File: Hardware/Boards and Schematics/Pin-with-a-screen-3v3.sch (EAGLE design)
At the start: 29 parts, among them J1 AVR_SPI_PRG_6NS, Q1 MMBT2222A, Q2 BL8530, U1 ATMEGA328P, U2 MICRO-SD-SOCKET-SMD1:1, Y1 8MHz

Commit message: Removed transistor-resistor logic level shifter
Logic level shifter was used for PWM-ing backlight signal for screen.
Since MCU operates on 3v3 logic like screen, level shifter is not
necessary.
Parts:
- removed Q1: MMBT2222A, SparkFun-DiscreteSemi:TRANSISTOR_NPNMMBT2222A
- removed R3: 1k, SparkFun-Passives:RESISTOR0603-RES
- removed R4: 22R, SparkFun-Passives:RESISTOR0603-RES
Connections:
- removed net LEDK: LCD2.LEDK, R4.2
- removed net TRAN_BASE: Q1.B, R3.2
- removed net TRAN_COLLECTOR: Q1.C, R4.1
- net GND: no longer Q1.E
- net TFT_BACKLIGHT: now also LCD2.LEDK; no longer R3.1
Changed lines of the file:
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@@
 <part name="C3" library="SparkFun" deviceset="CAP" device="0603-CAP" value="0.1uF"/>
 <part name="C4" library="SparkFun" deviceset="CAP" device="0603-CAP" value="0.1uF"/>
-<part name="Q1" library="SparkFun-DiscreteSemi" deviceset="TRANSISTOR_NPN" device="MMBT2222A" value="MMBT2222A"/>
-<part name="R3" library="SparkFun-Passives" deviceset="RESISTOR" device="0603-RES" value="1k"/>
-<part name="R4" library="SparkFun-Passives" deviceset="RESISTOR" device="0603-RES" value="22R"/>
-<part name="GND2" library="SparkFun-Aesthetics" deviceset="GND" device=""/>
 <part name="GND3" library="SparkFun-Aesthetics" deviceset="GND" device=""/>
 <part name="SUPPLY2" library="SparkFun-Aesthetics" deviceset="3.3V" device=""/>
@@
 <instance part="C3" gate="G$1" x="-119.38" y="154.94"/>
 <instance part="C4" gate="G$1" x="-104.14" y="154.94"/>
-<instance part="Q1" gate="G$1" x="-43.18" y="60.96" rot="MR0"/>
-<instance part="R3" gate="G$1" x="-35.56" y="68.58" rot="R180"/>
-<instance part="R4" gate="G$1" x="-71.12" y="66.04" rot="R180"/>
-<instance part="GND2" gate="1" x="-45.72" y="50.8"/>
 <instance part="GND3" gate="1" x="-111.76" y="147.32"/>
 <instance part="SUPPLY2" gate="G$1" x="-111.76" y="162.56"/>
@@
 <net name="GND" class="0">
 <segment>
-<pinref part="Q1" gate="G$1" pin="E"/>
-<pinref part="GND2" gate="1" pin="GND"/>
-<wire x1="-45.72" y1="55.88" x2="-45.72" y2="53.34" width="0.1524" layer="91"/>
-</segment>
-<segment>
 <pinref part="C3" gate="G$1" pin="2"/>
 <wire x1="-119.38" y1="152.4" x2="-119.38" y2="149.86" width="0.1524" layer="91"/>
@@
 </segment>
 </net>
-<net name="TRAN_COLLECTOR" class="0">
-<segment>
-<pinref part="R4" gate="G$1" pin="1"/>
-<pinref part="Q1" gate="G$1" pin="C"/>
-<wire x1="-66.04" y1="66.04" x2="-45.72" y2="66.04" width="0.1524" layer="91"/>
-</segment>
-</net>
-<net name="TRAN_BASE" class="0">
-<segment>
-<pinref part="R3" gate="G$1" pin="2"/>
-<pinref part="Q1" gate="G$1" pin="B"/>
-<wire x1="-40.64" y1="68.58" x2="-40.64" y2="60.96" width="0.1524" layer="91"/>
-</segment>
-</net>
 <net name="N$3" class="0">
 <segment>
@@
 </segment>
 <segment>
-<pinref part="R3" gate="G$1" pin="1"/>
-<wire x1="-30.48" y1="68.58" x2="-17.78" y2="68.58" width="0.1524" layer="91"/>
-<label x="-20.32" y="68.58" size="1.778" layer="95"/>
-</segment>
-</net>
-<net name="LEDK" class="0">
-<segment>
 <pinref part="LCD2" gate="G$1" pin="LEDK"/>
 <wire x1="-86.36" y1="48.26" x2="-76.2" y2="48.26" width="0.1524" layer="91"/>
-<wire x1="-76.2" y1="48.26" x2="-76.2" y2="66.04" width="0.1524" layer="91"/>
-<pinref part="R4" gate="G$1" pin="2"/>
-</segment>
-</net>
+<wire x1="-76.2" y1="48.26" x2="-76.2" y2="60.96" width="0.1524" layer="91"/>
+<wire x1="-76.2" y1="60.96" x2="-66.04" y2="60.96" width="0.1524" layer="91"/>
+<label x="-66.04" y="60.96" size="1.778" layer="95"/>
+</segment>
+</net>

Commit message: Changed led to red and series resistor to 51R
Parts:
- BLINKY: value Green -> Red
- R1: value 5R -> 51R
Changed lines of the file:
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@@
 <part name="SUPPLY9" library="SparkFun-Aesthetics" deviceset="3.3V" device=""/>
 <part name="GND9" library="SparkFun-Aesthetics" deviceset="GND" device=""/>
-<part name="R1" library="SparkFun-Passives" deviceset="RESISTOR" device="0603-RES" value="5R"/>
-<part name="BLINKY" library="SparkFun" deviceset="LED" device="0603" value="Green"/>
+<part name="R1" library="SparkFun-Passives" deviceset="RESISTOR" device="0603-RES" value="51R"/>
+<part name="BLINKY" library="SparkFun" deviceset="LED" device="0603" value="Red"/>
 <part name="GND13" library="SparkFun-Aesthetics" deviceset="GND" device=""/>
 <part name="PAD1" library="wirepad" deviceset="2,15/1,0" device=""/>

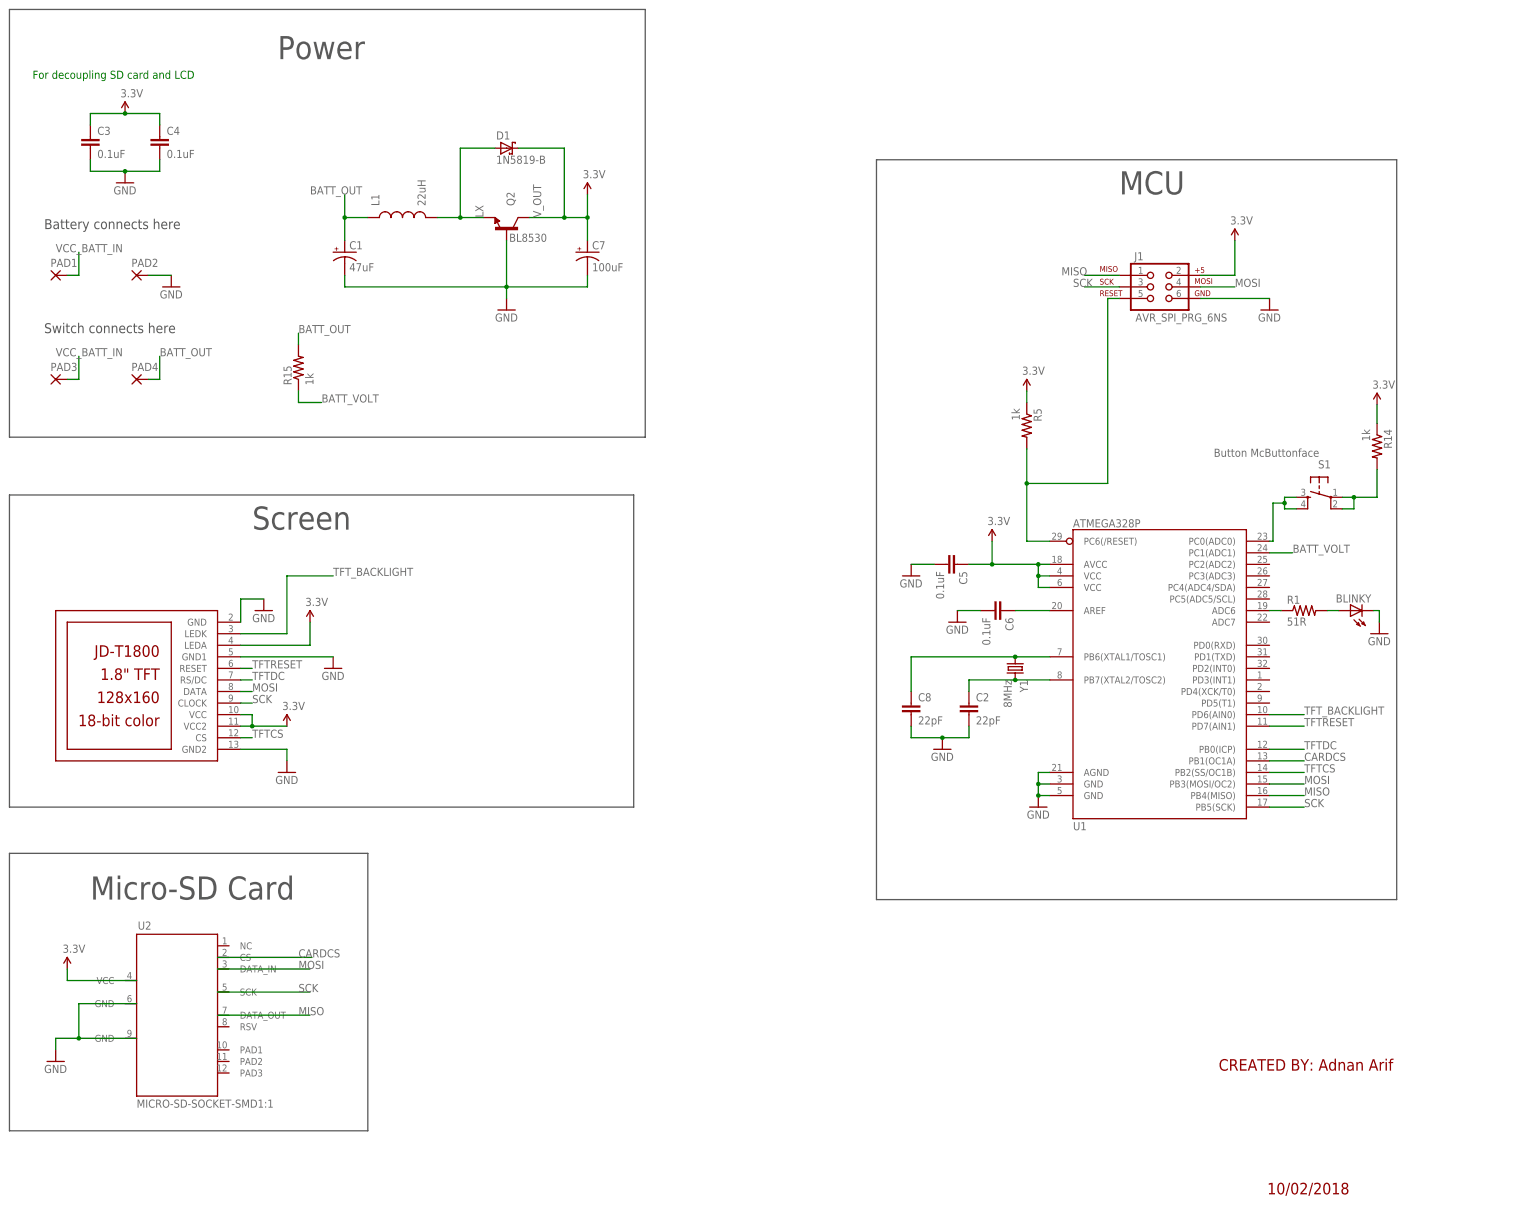
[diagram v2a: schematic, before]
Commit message: Added protoboard section
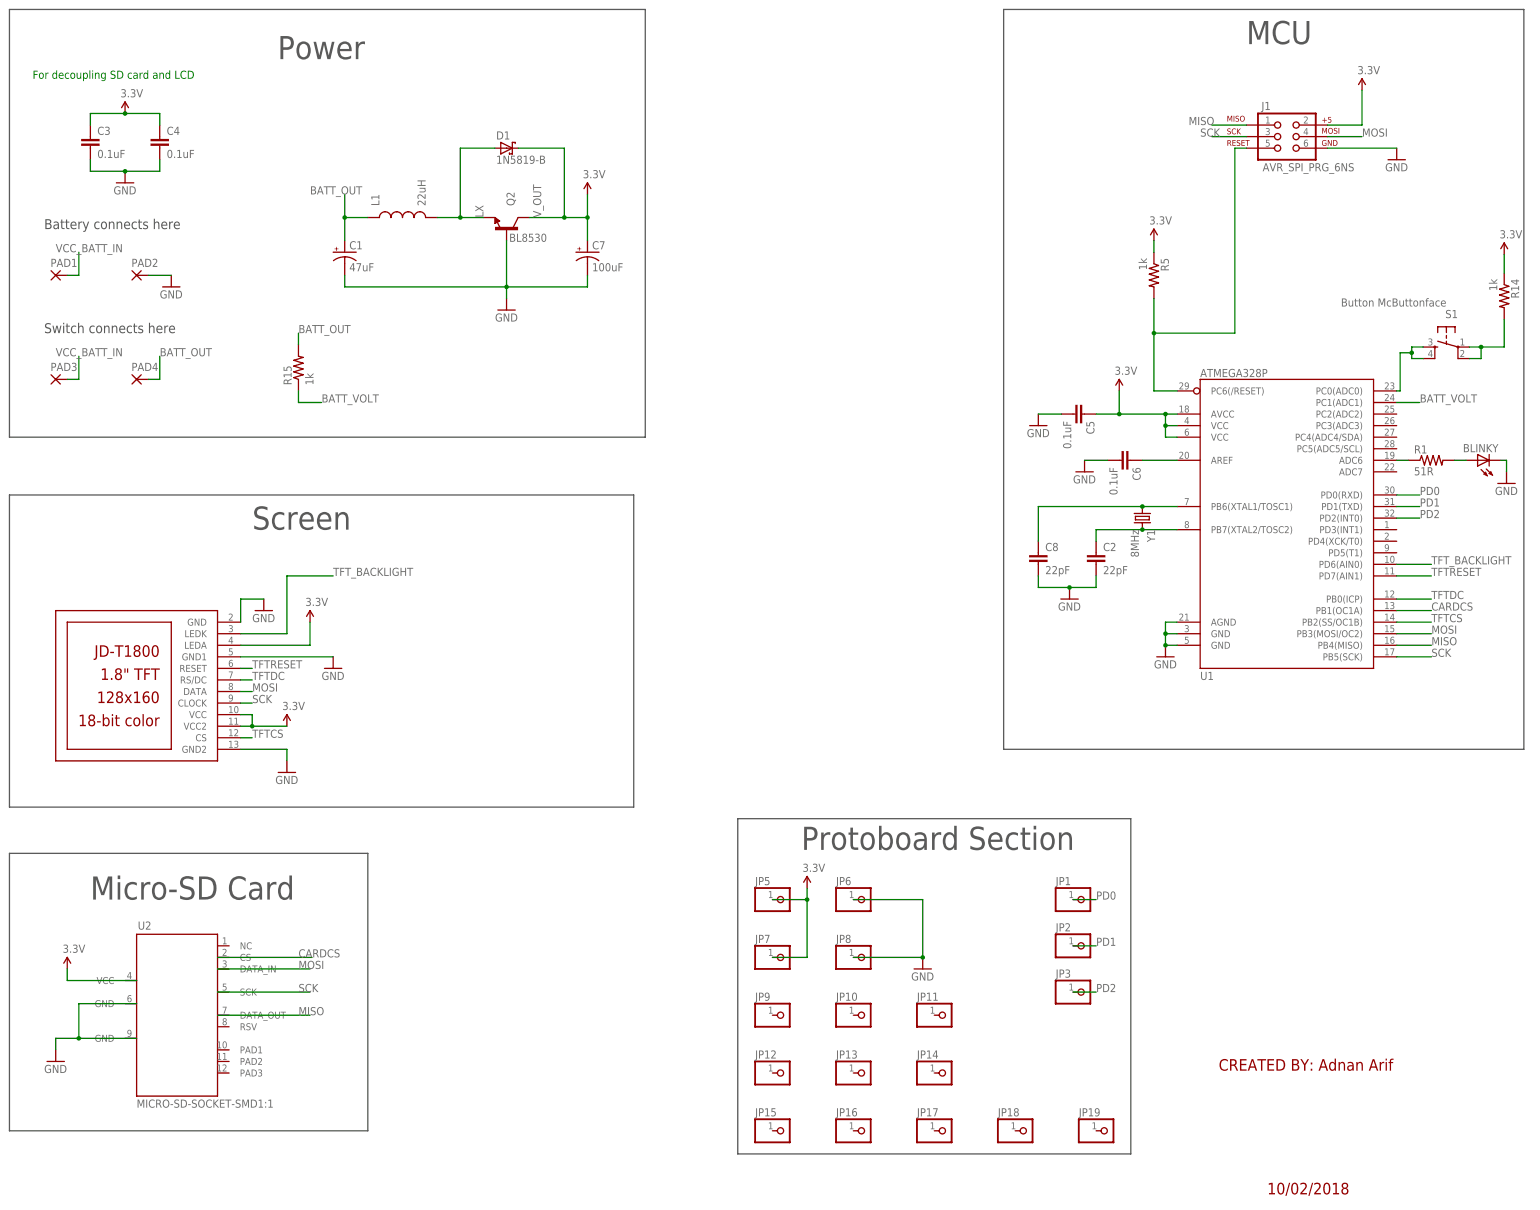
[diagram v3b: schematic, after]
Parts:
- added JP1, JP10, JP11, JP12, JP13, JP14, JP15, JP16, JP17, JP18, JP19, JP2, JP3, JP5, JP6, JP7, JP8, JP9: (no value), pinhead:PINHD-1X1
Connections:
- new net PD0: JP1.1, U1.PD0(RXD)
- new net PD1: JP2.1, U1.PD1(TXD)
- new net PD2: JP3.1, U1.PD2(INT0)
- net 3.3V: now also JP5.1, JP7.1
- net GND: now also JP6.1, JP8.1
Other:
- note added: "Protoboard Section"
- moved on the sheet: BLINKY, C2, C5, C6, C8, J1, R1, R14, R5, S1, U1, Y1

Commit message: Changed button to horizontal type, added screw-hole
Push button changed to horizontal with custom footprint. It replaced the
vertical push button. Some traces were re-routed to accomodate it.

Screw-hole added to bottom left of board since top left one could have
issues with push button.
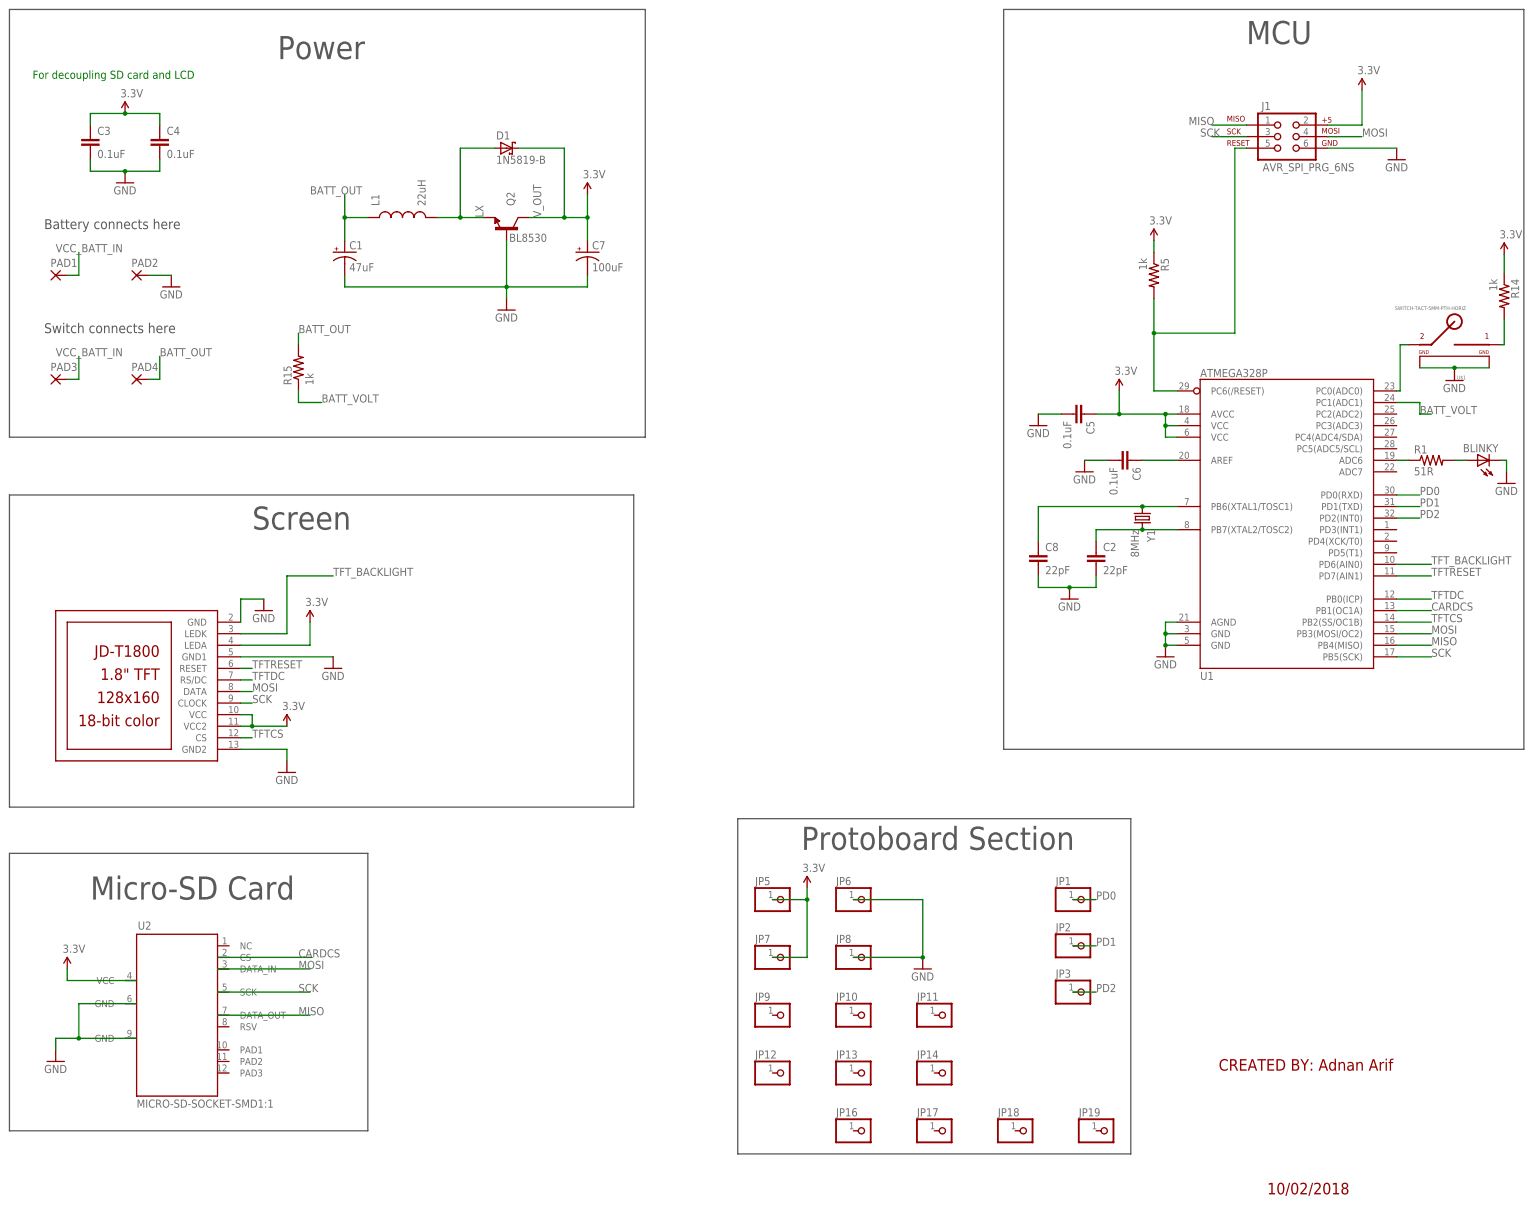
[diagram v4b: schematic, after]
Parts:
- removed JP15: (no value), pinhead:PINHD-1X1
- removed S1: Button McButtonface, SparkFun-Electromechanical:TAC_SWITCHPTH
- added U$1: SWITCH-TACT-5MM-PTH-HORIZ, switches_adnan:SWITCH-TACT-5MM-PTH-HORIZ
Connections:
- net GND: now also U$1.GND, U$1.GND1
- net N$1: now also U$1.2; no longer S1.3, S1.4
- net N$2: now also U$1.1; no longer S1.1, S1.2
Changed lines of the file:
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@@
 <part name="J1" library="SparkFun-Connectors" deviceset="AVR_SPI_PRG_6" device="NS"/>
 <part name="R5" library="SparkFun-Passives" deviceset="RESISTOR" device="0603-RES" value="1k"/>
-<part name="S1" library="SparkFun-Electromechanical" deviceset="TAC_SWITCH" device="PTH" value="Button McButtonface"/>
 <part name="GND8" library="SparkFun-Aesthetics" deviceset="GND" device=""/>
 <part name="GND10" library="SparkFun-Aesthetics" deviceset="GND" device=""/>
@@
 <part name="JP13" library="pinhead" deviceset="PINHD-1X1" device=""/>
 <part name="JP14" library="pinhead" deviceset="PINHD-1X1" device=""/>
-<part name="JP15" library="pinhead" deviceset="PINHD-1X1" device=""/>
 <part name="JP16" library="pinhead" deviceset="PINHD-1X1" device=""/>
 <part name="JP17" library="pinhead" deviceset="PINHD-1X1" device=""/>
@@
 <part name="JP2" library="pinhead" deviceset="PINHD-1X1" device=""/>
 <part name="JP3" library="pinhead" deviceset="PINHD-1X1" device=""/>
+<part name="U$1" library="switches_adnan" deviceset="SWITCH-TACT-5MM-PTH-HORIZ" device=""/>
+<part name="GND15" library="SparkFun-Aesthetics" deviceset="GND" device=""/>
 </parts>
 <sheets>
@@
 <instance part="J1" gate="G$1" x="142.24" y="157.48"/>
 <instance part="R5" gate="G$1" x="114.3" y="127" rot="R270"/>
-<instance part="S1" gate="S" x="178.562" y="111.252" smashed="yes" rot="MR0">
-<attribute name="NAME" x="181.102" y="117.602" size="1.778" layer="95" rot="MR0"/>
-<attribute name="VALUE" x="178.562" y="120.142" size="1.778" layer="96" rot="MR0"/>
-</instance>
 <instance part="GND8" gate="1" x="167.64" y="152.4"/>
 <instance part="GND10" gate="1" x="-81.28" y="53.34"/>
@@
 <instance part="JP13" gate="G$1" x="50.8" y="-48.26"/>
 <instance part="JP14" gate="G$1" x="68.58" y="-48.26"/>
-<instance part="JP15" gate="G$1" x="33.02" y="-60.96"/>
 <instance part="JP16" gate="G$1" x="50.8" y="-60.96"/>
 <instance part="JP17" gate="G$1" x="68.58" y="-60.96"/>
@@
 <instance part="JP2" gate="G$1" x="99.06" y="-20.32"/>
 <instance part="JP3" gate="G$1" x="99.06" y="-30.48"/>
+<instance part="U$1" gate="G$1" x="180.34" y="111.76" rot="MR0"/>
+<instance part="GND15" gate="1" x="180.34" y="103.886"/>
 </instances>
 <busses>
@@
 <pinref part="JP8" gate="G$1" pin="1"/>
 </segment>
+<segment>
+<pinref part="U$1" gate="G$1" pin="GND1"/>
+<pinref part="U$1" gate="G$1" pin="GND"/>
+<wire x1="172.72" y1="106.68" x2="180.34" y2="106.68" width="0.1524" layer="91"/>
+<pinref part="GND15" gate="1" pin="GND"/>
+<wire x1="180.34" y1="106.68" x2="187.96" y2="106.68" width="0.1524" layer="91"/>
+<wire x1="180.34" y1="106.426" x2="180.34" y2="106.68" width="0.1524" layer="91"/>
+<junction x="180.34" y="106.68"/>
+</segment>
 </net>
 <net name="N$3" class="0">
@@
 <net name="N$1" class="0">
 <segment>
-<pinref part="S1" gate="S" pin="4"/>
-<pinref part="S1" gate="S" pin="3"/>
-<wire x1="173.482" y1="111.252" x2="170.942" y2="111.252" width="0.1524" layer="91"/>
-<wire x1="170.942" y1="111.252" x2="170.942" y2="109.982" width="0.1524" layer="91"/>
-<wire x1="170.942" y1="109.982" x2="170.942" y2="108.712" width="0.1524" layer="91"/>
-<wire x1="170.942" y1="108.712" x2="173.482" y2="108.712" width="0.1524" layer="91"/>
-<wire x1="170.942" y1="109.982" x2="168.402" y2="109.982" width="0.1524" layer="91"/>
-<wire x1="168.402" y1="109.982" x2="168.402" y2="101.6" width="0.1524" layer="91"/>
-<junction x="170.942" y="109.982"/>
+<wire x1="168.402" y1="111.76" x2="168.402" y2="101.6" width="0.1524" layer="91"/>
 <pinref part="U1" gate="G$1" pin="PC0(ADC0)"/>
 <wire x1="168.402" y1="101.6" x2="167.64" y2="101.6" width="0.1524" layer="91"/>
-</segment>
-</net>
-<net name="N$2" class="0">
-<segment>
-<pinref part="S1" gate="S" pin="1"/>
-<wire x1="183.642" y1="111.252" x2="186.182" y2="111.252" width="0.1524" layer="91"/>
-<wire x1="186.182" y1="111.252" x2="191.262" y2="111.252" width="0.1524" layer="91"/>
-<wire x1="186.182" y1="111.252" x2="186.182" y2="108.712" width="0.1524" layer="91"/>
-<junction x="186.182" y="111.252"/>
-<pinref part="S1" gate="S" pin="2"/>
-<wire x1="186.182" y1="108.712" x2="183.642" y2="108.712" width="0.1524" layer="91"/>
-<pinref part="R14" gate="G$1" pin="2"/>
-<wire x1="191.262" y1="117.348" x2="191.262" y2="111.252" width="0.1524" layer="91"/>
+<pinref part="U$1" gate="G$1" pin="2"/>
+<wire x1="170.18" y1="111.76" x2="168.402" y2="111.76" width="0.1524" layer="91"/>
 </segment>
 </net>
@@
 <pinref part="U1" gate="G$1" pin="PC1(ADC1)"/>
 <wire x1="167.64" y1="99.06" x2="172.72" y2="99.06" width="0.1524" layer="91"/>
-<label x="172.72" y="99.06" size="1.778" layer="95"/>
+<label x="172.72" y="96.52" size="1.778" layer="95"/>
+<wire x1="172.72" y1="99.06" x2="172.72" y2="96.52" width="0.1524" layer="91"/>
+<wire x1="172.72" y1="96.52" x2="175.26" y2="96.52" width="0.1524" layer="91"/>
 </segment>
 </net>
@@
 </segment>
 </net>
+<net name="N$2" class="0">
+<segment>
+<pinref part="R14" gate="G$1" pin="2"/>
+<wire x1="191.262" y1="117.348" x2="191.262" y2="111.76" width="0.1524" layer="91"/>
+<pinref part="U$1" gate="G$1" pin="1"/>
+<wire x1="191.262" y1="111.76" x2="190.5" y2="111.76" width="0.1524" layer="91"/>
+</segment>
+</net>
